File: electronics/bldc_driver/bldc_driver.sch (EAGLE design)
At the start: 28 parts, among them Q1 MOSFET-N, Q2 MOSFET-N, Q3 MOSFET-N, Q4 MOSFET-N, Q5 MOSFET-N, Q6 MOSFET-N

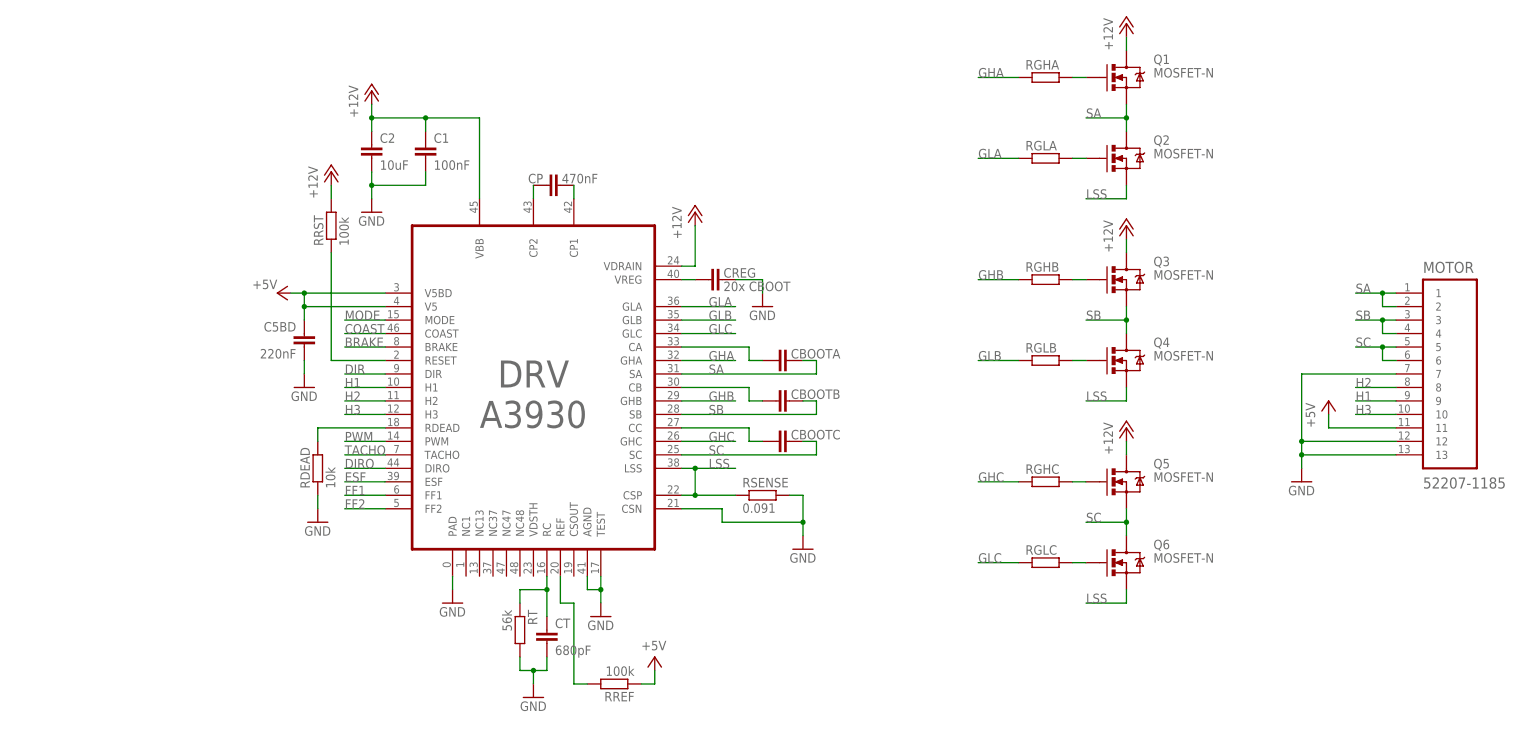
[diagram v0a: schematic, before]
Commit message: Started routing motor driver board
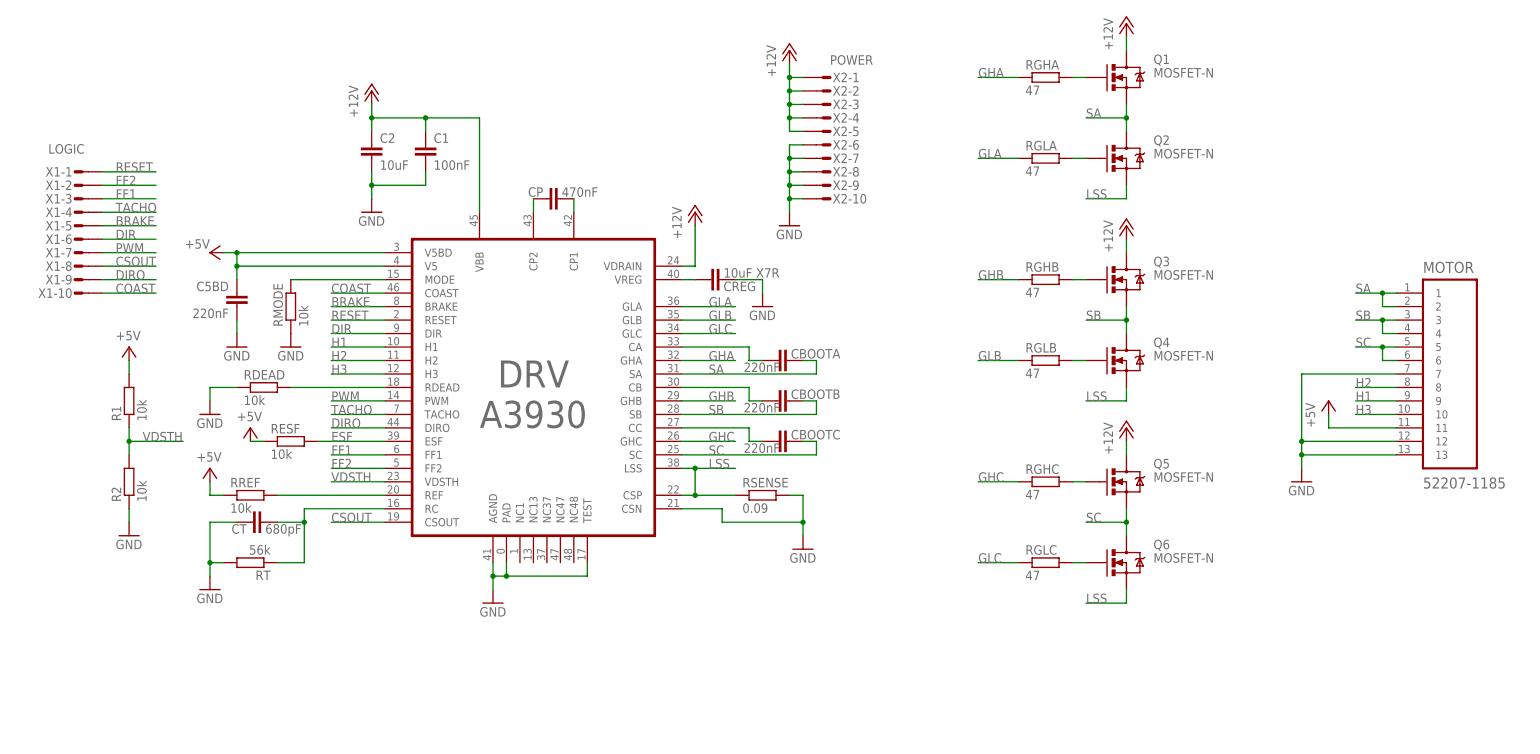
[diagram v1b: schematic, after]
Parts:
- removed RRST: 100k, rcl:R-EU_R0603
- added R1, R2, RESF, RMODE: 10k, rcl:R-EU_R0603
- added X1: LOGIC, con-amp-micromatch:MICROMATCH-10
- added X2: POWER, con-amp-micromatch:MICROMATCH-10
- C1: device rcl:C-EUC0603K -> rcl:C-EUC0603
- CBOOTA, CBOOTB, CBOOTC: value (none) -> 220nF
- CREG: value 20x CBOOT -> 10uF X7R; device rcl:C-EUC0603 -> rcl:C-EUC1206K
- RGHA, RGHB, RGHC, RGLA, RGLB, RGLC: value (none) -> 47
- RREF: value 100k -> 10k
- RSENSE: value 0.091 -> 0.09; device rcl:R-EU_R0603 -> rcl:R-EU_R2010
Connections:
- removed net MODE: DRV.MODE
- removed net N$16: DRV.RESET, RRST.1
- new net CSOUT: DRV.CSOUT, X1-8.S
- new net N$18: DRV.MODE, RMODE.2
- new net RESET: DRV.RESET, X1-1.S
- new net VDSTH: DRV.VDSTH, R1.1, R2.2
- net +12V: now also X2-1.S, X2-2.S, X2-3.S, X2-4.S, X2-5.S; no longer RRST.2
- net +5V: now also R1.2, RESF.1
- net BRAKE: now also X1-5.S
- net COAST: now also X1-10.S
- net DIR: now also X1-6.S
- net DIRO: now also X1-9.S
- net ESF: now also RESF.2
- net FF1: now also X1-3.S
- net FF2: now also X1-2.S
- net GND: now also CREG.2, R2.1, RMODE.1, X2-10.S, X2-6.S, X2-7.S, X2-8.S, X2-9.S; no longer CREG.1
- net N$8: now also CREG.1; no longer CREG.2
- net PWM: now also X1-7.S
- net TACHO: now also X1-4.S
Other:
- moved on the sheet: C5BD, CP, CREG, CT, RDEAD, RREF, RT

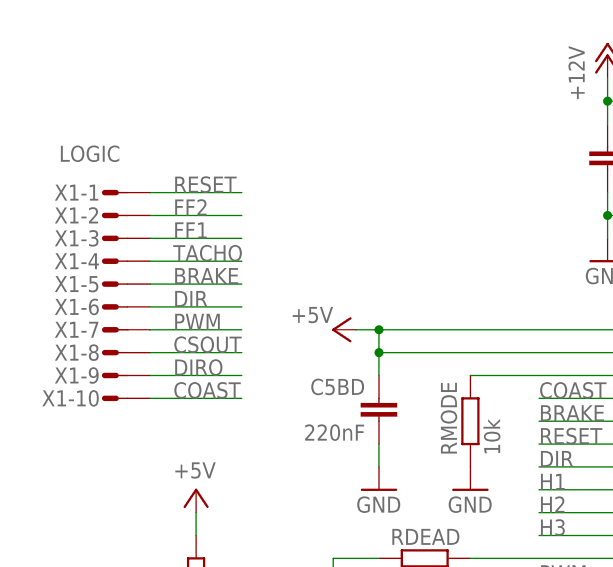
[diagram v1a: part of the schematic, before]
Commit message: Routed motor driver board
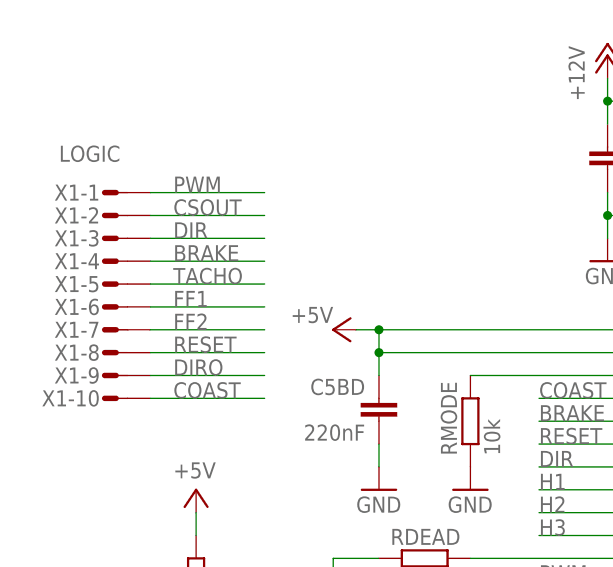
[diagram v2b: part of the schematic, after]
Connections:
- net BRAKE: now also X1-4.S; no longer X1-5.S
- net CSOUT: now also X1-2.S; no longer X1-8.S
- net DIR: now also X1-3.S; no longer X1-6.S
- net FF1: now also X1-6.S; no longer X1-3.S
- net FF2: now also X1-7.S; no longer X1-2.S
- net PWM: now also X1-1.S; no longer X1-7.S
- net RESET: now also X1-8.S; no longer X1-1.S
- net TACHO: now also X1-5.S; no longer X1-4.S
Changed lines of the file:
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@@
 </segment>
 <segment>
-<pinref part="X1" gate="-6" pin="S"/>
-<wire x1="-35.56" y1="73.66" x2="-25.4" y2="73.66" width="0.1524" layer="91"/>
-<label x="-33.02" y="73.66" size="1.778" layer="95"/>
+<pinref part="X1" gate="-3" pin="S"/>
+<wire x1="-35.56" y1="81.28" x2="-22.86" y2="81.28" width="0.1524" layer="91"/>
+<label x="-33.02" y="81.28" size="1.778" layer="95"/>
 </segment>
 </net>
@@
 <segment>
 <pinref part="X1" gate="-10" pin="S"/>
-<wire x1="-35.56" y1="63.5" x2="-25.4" y2="63.5" width="0.1524" layer="91"/>
+<wire x1="-35.56" y1="63.5" x2="-22.86" y2="63.5" width="0.1524" layer="91"/>
 <label x="-33.02" y="63.5" size="1.778" layer="95"/>
 </segment>
@@
 </segment>
 <segment>
-<pinref part="X1" gate="-7" pin="S"/>
-<wire x1="-35.56" y1="71.12" x2="-25.4" y2="71.12" width="0.1524" layer="91"/>
-<label x="-33.02" y="71.12" size="1.778" layer="95"/>
+<pinref part="X1" gate="-1" pin="S"/>
+<wire x1="-35.56" y1="86.36" x2="-22.86" y2="86.36" width="0.1524" layer="91"/>
+<label x="-33.02" y="86.36" size="1.778" layer="95"/>
 </segment>
 </net>
@@
 </segment>
 <segment>
-<pinref part="X1" gate="-4" pin="S"/>
-<wire x1="-35.56" y1="78.74" x2="-25.4" y2="78.74" width="0.1524" layer="91"/>
-<label x="-33.02" y="78.74" size="1.778" layer="95"/>
+<pinref part="X1" gate="-5" pin="S"/>
+<wire x1="-35.56" y1="76.2" x2="-22.86" y2="76.2" width="0.1524" layer="91"/>
+<label x="-33.02" y="76.2" size="1.778" layer="95"/>
 </segment>
 </net>
@@
 <segment>
 <pinref part="X1" gate="-9" pin="S"/>
-<wire x1="-35.56" y1="66.04" x2="-25.4" y2="66.04" width="0.1524" layer="91"/>
+<wire x1="-35.56" y1="66.04" x2="-22.86" y2="66.04" width="0.1524" layer="91"/>
 <label x="-33.02" y="66.04" size="1.778" layer="95"/>
 </segment>
@@
 </segment>
 <segment>
-<pinref part="X1" gate="-3" pin="S"/>
-<wire x1="-35.56" y1="81.28" x2="-25.4" y2="81.28" width="0.1524" layer="91"/>
-<label x="-33.02" y="81.28" size="1.778" layer="95"/>
+<pinref part="X1" gate="-6" pin="S"/>
+<wire x1="-35.56" y1="73.66" x2="-22.86" y2="73.66" width="0.1524" layer="91"/>
+<label x="-33.02" y="73.66" size="1.778" layer="95"/>
 </segment>
 </net>
@@
 </segment>
 <segment>
-<pinref part="X1" gate="-2" pin="S"/>
-<wire x1="-35.56" y1="83.82" x2="-25.4" y2="83.82" width="0.1524" layer="91"/>
-<label x="-33.02" y="83.82" size="1.778" layer="95"/>
+<pinref part="X1" gate="-7" pin="S"/>
+<wire x1="-35.56" y1="71.12" x2="-22.86" y2="71.12" width="0.1524" layer="91"/>
+<label x="-33.02" y="71.12" size="1.778" layer="95"/>
 </segment>
 </net>
@@
 </segment>
 <segment>
-<pinref part="X1" gate="-8" pin="S"/>
-<wire x1="-35.56" y1="68.58" x2="-25.4" y2="68.58" width="0.1524" layer="91"/>
-<label x="-33.02" y="68.58" size="1.778" layer="95"/>
+<pinref part="X1" gate="-2" pin="S"/>
+<wire x1="-35.56" y1="83.82" x2="-22.86" y2="83.82" width="0.1524" layer="91"/>
+<label x="-33.02" y="83.82" size="1.778" layer="95"/>
 </segment>
 </net>
 <net name="RESET" class="0">
 <segment>
-<pinref part="X1" gate="-1" pin="S"/>
-<wire x1="-35.56" y1="86.36" x2="-25.4" y2="86.36" width="0.1524" layer="91"/>
-<label x="-33.02" y="86.36" size="1.778" layer="95"/>
-</segment>
-<segment>
 <pinref part="DRV" gate="G$1" pin="RESET"/>
 <wire x1="17.78" y1="58.42" x2="7.62" y2="58.42" width="0.1524" layer="91"/>
 <label x="7.62" y="58.42" size="1.778" layer="95"/>
+</segment>
+<segment>
+<pinref part="X1" gate="-8" pin="S"/>
+<wire x1="-35.56" y1="68.58" x2="-22.86" y2="68.58" width="0.1524" layer="91"/>
+<label x="-33.02" y="68.58" size="1.778" layer="95"/>
 </segment>
 </net>
@@
 </segment>
 <segment>
-<pinref part="X1" gate="-5" pin="S"/>
-<wire x1="-35.56" y1="76.2" x2="-25.4" y2="76.2" width="0.1524" layer="91"/>
-<label x="-33.02" y="76.2" size="1.778" layer="95"/>
+<pinref part="X1" gate="-4" pin="S"/>
+<wire x1="-35.56" y1="78.74" x2="-22.86" y2="78.74" width="0.1524" layer="91"/>
+<label x="-33.02" y="78.74" size="1.778" layer="95"/>
 </segment>
 </net>

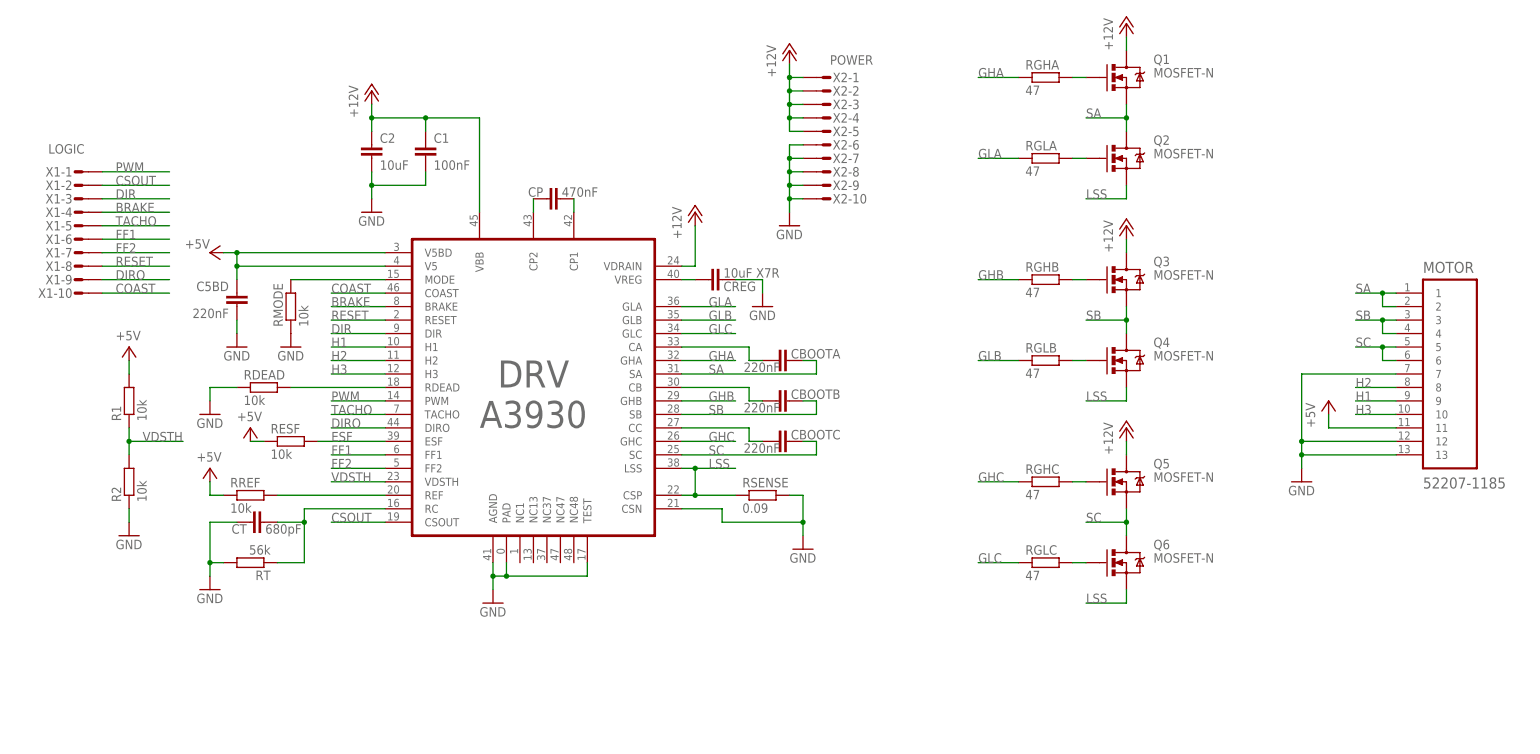
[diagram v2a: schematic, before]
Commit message: Added pass through transistor for +5V, added +5V and fault LEDs, separated driver and noisy ground with 1 ohm resistor, added 2 GNDs to logic connector, added holes for micro-match connectors
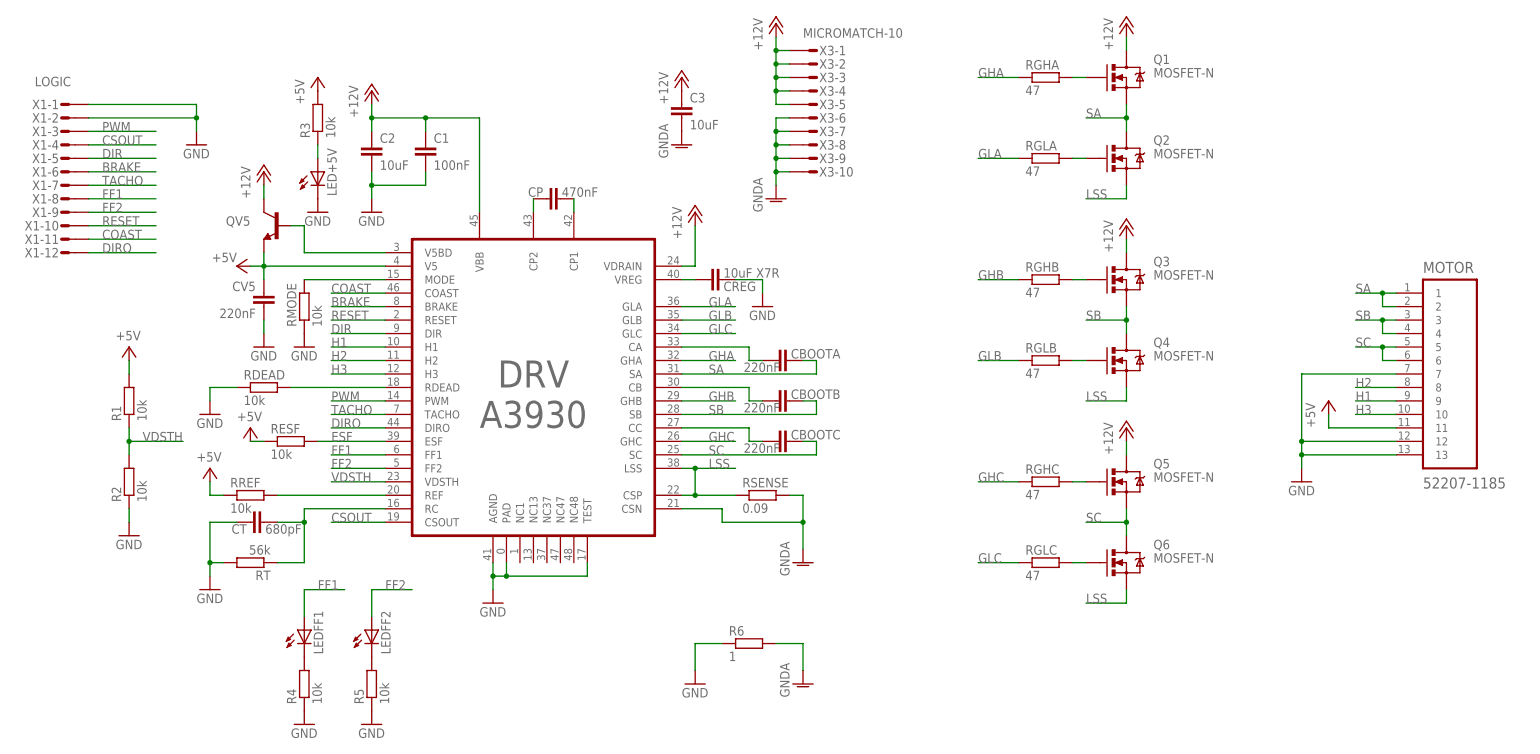
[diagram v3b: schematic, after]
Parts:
- removed C5BD: 220nF, rcl:C-EUC0603
- removed X2: POWER, con-amp-micromatch:MICROMATCH-10
- added C3: 10uF, rcl:C-EUC1206K
- added CV5: 220nF, rcl:C-EUC0603
- added LED+5V, LEDFF1, LEDFF2: (no value), led:LEDCHIPLED_0603
- added QV5: (no value), SparkFun-DiscreteSemi:TRANSISTOR_NPNSOT23
- added R3, R4, R5: 10k, rcl:R-EU_R0603
- added R6: 1, rcl:R-EU_R0603
- added X3: MICROMATCH-10, con-amp-micromatch:MICROMATCH-10
- X1: device con-amp-micromatch:MICROMATCH-10 -> con-amp-micromatch:MICROMATCH-12
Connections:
- new net GNDA: C3.2, DRV.CSN, R6.2, RSENSE.2, X3-10.S, X3-6.S, X3-7.S, X3-8.S, X3-9.S
- new net N$16: LED+5V.A, R3.1
- new net N$19: LEDFF1.C, R4.2
- new net N$20: LEDFF2.C, R5.2
- new net N$21: DRV.V5BD, QV5.B
- net +12V: now also C3.1, QV5.C, X3-1.S, X3-2.S, X3-3.S, X3-4.S, X3-5.S; no longer X2-1.S, X2-2.S, X2-3.S, X2-4.S, X2-5.S
- net +5V: now also CV5.2, QV5.E, R3.2; no longer C5BD.2, DRV.V5BD
- net BRAKE: now also X1-6.S; no longer X1-4.S
- net COAST: now also X1-11.S; no longer X1-10.S
- net CSOUT: now also X1-4.S; no longer X1-2.S
- net DIR: now also X1-5.S; no longer X1-3.S
- net DIRO: now also X1-12.S; no longer X1-9.S
- net FF1: now also LEDFF1.A, X1-8.S; no longer X1-6.S
- net FF2: now also LEDFF2.A, X1-9.S; no longer X1-7.S
- net GND: now also CV5.1, LED+5V.C, R4.1, R5.1, R6.1, X1-1.S, X1-2.S; no longer C5BD.1, DRV.CSN, RSENSE.2, X2-10.S, X2-6.S, X2-7.S, X2-8.S, X2-9.S
- net PWM: now also X1-3.S; no longer X1-1.S
- net RESET: now also X1-10.S; no longer X1-8.S
- net TACHO: now also X1-7.S; no longer X1-5.S
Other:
- moved on the sheet: RMODE, X1-1, X1-10, X1-2, X1-3, X1-4, X1-5, X1-6, X1-7, X1-8, X1-9

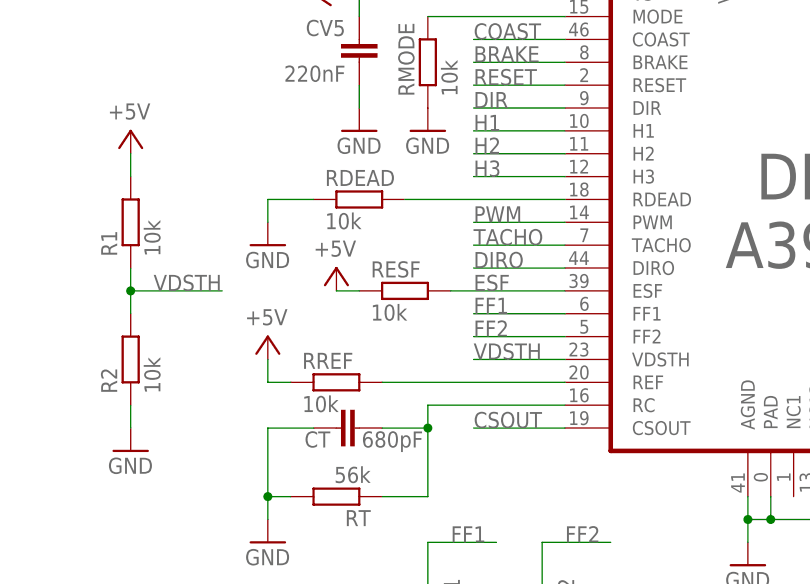
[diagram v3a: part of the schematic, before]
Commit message: Changed motor driver board logic connector position a bit
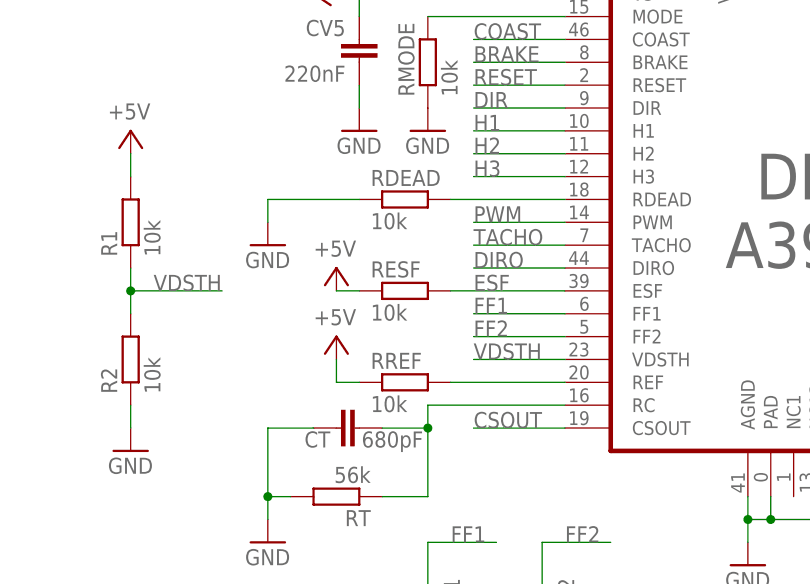
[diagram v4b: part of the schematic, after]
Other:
- moved on the sheet: RDEAD, RREF
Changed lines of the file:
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@@
 <attribute name="VALUE" x="-6.604" y="60.579" size="1.778" layer="96" rot="R180"/>
 </instance>
-<instance part="RDEAD" gate="G$1" x="-5.08" y="45.72"/>
+<instance part="RDEAD" gate="G$1" x="0" y="45.72"/>
 <instance part="GND2" gate="1" x="-15.24" y="40.64"/>
-<instance part="RREF" gate="G$1" x="-7.62" y="25.4"/>
-<instance part="P+10" gate="1" x="-15.24" y="30.48" smashed="yes">
-<attribute name="VALUE" x="-17.78" y="31.75" size="1.778" layer="96"/>
+<instance part="RREF" gate="G$1" x="0" y="25.4"/>
+<instance part="P+10" gate="1" x="-7.62" y="30.48" smashed="yes">
+<attribute name="VALUE" x="-10.16" y="31.75" size="1.778" layer="96"/>
 </instance>
 <instance part="C2" gate="G$1" x="15.24" y="91.44"/>
@@
 <pinref part="GND2" gate="1" pin="GND"/>
 <wire x1="-15.24" y1="43.18" x2="-15.24" y2="45.72" width="0.1524" layer="91"/>
-<wire x1="-15.24" y1="45.72" x2="-10.16" y2="45.72" width="0.1524" layer="91"/>
+<wire x1="-15.24" y1="45.72" x2="-5.08" y2="45.72" width="0.1524" layer="91"/>
 </segment>
 <segment>
@@
 <segment>
 <pinref part="P+10" gate="1" pin="+5V"/>
-<wire x1="-15.24" y1="27.94" x2="-15.24" y2="25.4" width="0.1524" layer="91"/>
+<wire x1="-7.62" y1="27.94" x2="-7.62" y2="25.4" width="0.1524" layer="91"/>
 <pinref part="RREF" gate="G$1" pin="1"/>
-<wire x1="-15.24" y1="25.4" x2="-12.7" y2="25.4" width="0.1524" layer="91"/>
+<wire x1="-7.62" y1="25.4" x2="-5.08" y2="25.4" width="0.1524" layer="91"/>
 </segment>
 <segment>
@@
 <segment>
 <pinref part="DRV" gate="G$1" pin="RDEAD"/>
-<wire x1="17.78" y1="45.72" x2="0" y2="45.72" width="0.1524" layer="91"/>
+<wire x1="17.78" y1="45.72" x2="5.08" y2="45.72" width="0.1524" layer="91"/>
 <pinref part="RDEAD" gate="G$1" pin="2"/>
 </segment>
@@
 <segment>
 <pinref part="DRV" gate="G$1" pin="REF"/>
-<wire x1="17.78" y1="25.4" x2="-2.54" y2="25.4" width="0.1524" layer="91"/>
+<wire x1="17.78" y1="25.4" x2="5.08" y2="25.4" width="0.1524" layer="91"/>
 <pinref part="RREF" gate="G$1" pin="2"/>
 </segment>
